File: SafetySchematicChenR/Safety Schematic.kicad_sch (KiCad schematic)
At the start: 48 parts, among them J1 XT60-M, J2 430450200, J3 Conn_01x04_Pin, J4 22035035, J5 430450200, J6 430450200, J7 XT60-M, K1 Fujitsu_FTR-LYAA005x, Q1 IRLML6344TRPBF, U1 74AHC1G32, U10 MCP2562-E/P, U11 74AHC1G08, U12 MCP6286T-E/OT, U13 MAX603, U2 74LVC1GU04DRL, U3 LT1962-3, U4 MAX603, U5 74LVC1GU04DRL, U6 Inverter_Schmitt_Dual, U7 74LS279, U8 74LVC1GU04DRL

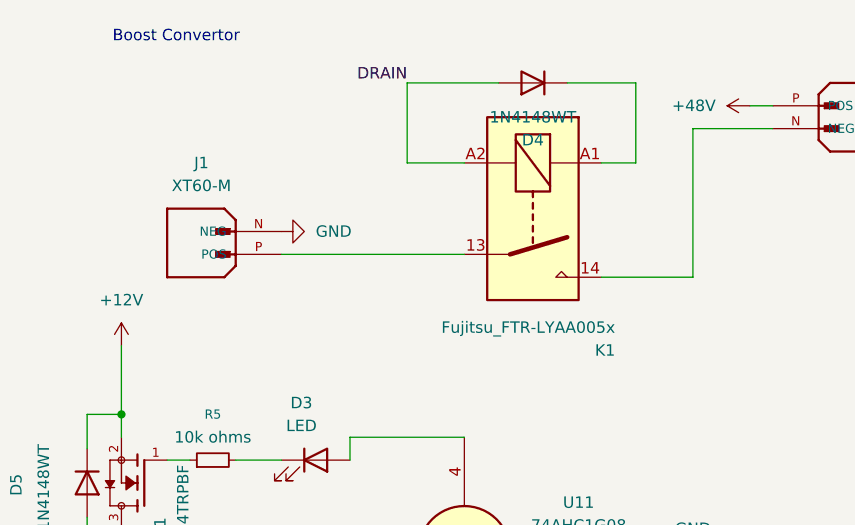
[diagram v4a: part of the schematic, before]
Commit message: replaced relay
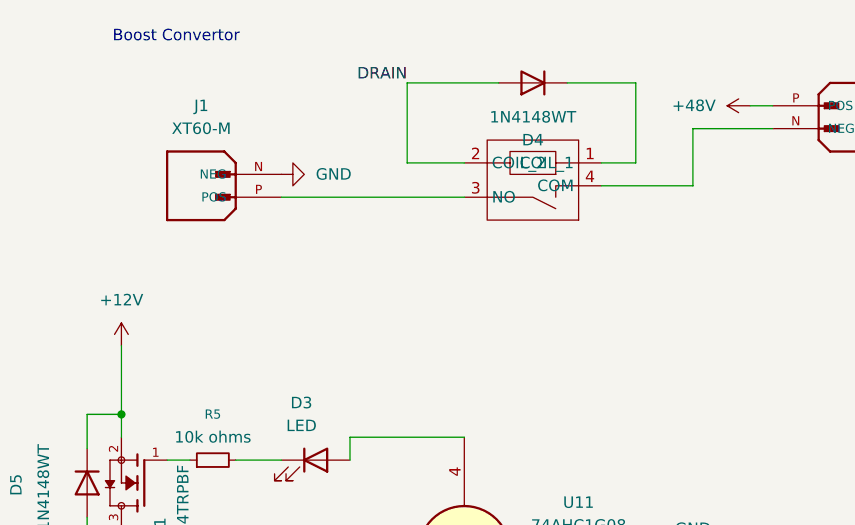
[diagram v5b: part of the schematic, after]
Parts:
- removed K1: Fujitsu_FTR-LYAA005x, Relay_THT:Relay_SPST-NO_Fujitsu_FTR-LYAA005x_FormA_Vertical, symbol Relay:Fujitsu_FTR-LYAA005x
- added U14: J115F11AH12VDCS61.5U, SMV_ICs:J115F11AH12VDCS615U, symbol SMV_Custom:J115F11AH12VDCS61.5U
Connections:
- net DRAIN: now also U14.2 (COIL_2)
- net at D4.1 (K): now also U14.1 (COIL_1)
- net at J1.P (POS): now also U14.3 (NO)
- net at J7.N (NEG): now also U14.4 (COM)
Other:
- moved on the sheet: J1
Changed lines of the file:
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@@
 	(wire
 		(pts
-			(xy 81.28 41.91) (xy 81.28 25.4)
+			(xy 81.28 31.75) (xy 81.28 25.4)
 		)
 		(stroke
@@
 	(wire
 		(pts
-			(xy 71.12 41.91) (xy 81.28 41.91)
+			(xy 71.12 31.75) (xy 81.28 31.75)
 		)
 		(stroke
@@
 	(wire
 		(pts
-			(xy 35.56 39.37) (xy 55.88 39.37)
+			(xy 35.56 33.02) (xy 55.88 33.02)
 		)
 		(stroke
@@
 	(symbol
 		(lib_id "power:GND")
-		(at 35.56 36.83 90)
+		(at 35.56 30.48 90)
 		(unit 1)
 		(exclude_from_sim no)
@@
 		(fields_autoplaced yes)
 		(property "Reference" "#PWR010"
-			(at 41.91 36.83 0)
+			(at 41.91 30.48 0)
 			(effects
 				(font
@@
 		)
 		(property "Value" "GND"
-			(at 39.37 36.8299 90)
+			(at 39.37 30.4799 90)
 			(effects
 				(font
@@
 		)
 		(property "Footprint" ""
-			(at 35.56 36.83 0)
+			(at 35.56 30.48 0)
 			(effects
 				(font
@@
 		)
 		(property "Datasheet" ""
-			(at 35.56 36.83 0)
+			(at 35.56 30.48 0)
 			(effects
 				(font
@@
 		)
 		(property "Description" "Power symbol creates a global label with name \"GND\" , ground"
-			(at 35.56 36.83 0)
+			(at 35.56 30.48 0)
 			(effects
 				(font
@@
 	(symbol
 		(lib_id "SMV_Custom:XT60-M")
-		(at 30.48 36.83 180)
+		(at 30.48 30.48 180)
 		(unit 1)
 		(exclude_from_sim no)
@@
 		(fields_autoplaced yes)
 		(property "Reference" "J1"
-			(at 26.67 29.21 0)
+			(at 26.67 22.86 0)
 			(effects
 				(font
@@
 		)
 		(property "Value" "XT60-M"
-			(at 26.67 31.75 0)
+			(at 26.67 25.4 0)
 			(effects
 				(font
@@
 		)
 		(property "Footprint" "SMV_Connectors:AMASS_XT60-M"
-			(at 30.48 36.83 0)
+			(at 30.48 30.48 0)
 			(effects
 				(font
@@
 		)
 		(property "Datasheet" ""
-			(at 30.48 36.83 0)
+			(at 30.48 30.48 0)
 			(effects
 				(font
@@
 		)
 		(property "Description" ""
-			(at 30.48 36.83 0)
+			(at 30.48 30.48 0)
 			(effects
 				(font
@@
 		)
 		(property "MF" "AMASS"
-			(at 30.48 36.83 0)
+			(at 30.48 30.48 0)
 			(effects
 				(font
@@
 		)
 		(property "MAXIMUM_PACKAGE_HEIGHT" "16.00 mm"
-			(at 30.48 36.83 0)
+			(at 30.48 30.48 0)
 			(effects
 				(font
@@
 		)
 		(property "Package" "Package"
-			(at 30.48 36.83 0)
+			(at 30.48 30.48 0)
 			(effects
 				(font
@@
 		)
 		(property "Price" "None"
-			(at 30.48 36.83 0)
+			(at 30.48 30.48 0)
 			(effects
 				(font
@@
 		)
 		(property "Check_prices" "https://www.snapeda.com/parts/XT60-M/AMASS/view-part/?ref=eda"
-			(at 30.48 36.83 0)
+			(at 30.48 30.48 0)
 			(effects
 				(font
@@
 		)
 		(property "STANDARD" "IPC 7351B"
-			(at 30.48 36.83 0)
+			(at 30.48 30.48 0)
 			(effects
 				(font
@@
 		)
 		(property "PARTREV" "V1.2"
-			(at 30.48 36.83 0)
+			(at 30.48 30.48 0)
 			(effects
 				(font
@@
 		)
 		(property "SnapEDA_Link" "https://www.snapeda.com/parts/XT60-M/AMASS/view-part/?ref=snap"
-			(at 30.48 36.83 0)
+			(at 30.48 30.48 0)
 			(effects
 				(font
@@
 		)
 		(property "MP" "XT60-M"
-			(at 30.48 36.83 0)
+			(at 30.48 30.48 0)
 			(effects
 				(font
@@
 		)
 		(property "Description_1" "\n                        \n                            Plug; DC supply; XT60; male; PIN: 2; for cable; soldered; 30A; 500V\n                        \n"
-			(at 30.48 36.83 0)
+			(at 30.48 30.48 0)
 			(effects
 				(font
@@
 		)
 		(property "Availability" "Not in stock"
-			(at 30.48 36.83 0)
+			(at 30.48 30.48 0)
 			(effects
 				(font
@@
 		)
 		(property "MANUFACTURER" "AMASS"
-			(at 30.48 36.83 0)
+			(at 30.48 30.48 0)
 			(effects
 				(font
@@
 	)
 	(symbol
-		(lib_id "Relay:Fujitsu_FTR-LYAA005x")
-		(at 63.5 34.29 270)
-		(unit 1)
-		(exclude_from_sim no)
-		(in_bom yes)
-		(on_board yes)
-		(dnp no)
-		(property "Reference" "K1"
-			(at 72.644 50.038 90)
-			(effects
-				(font
-					(size 1.27 1.27)
-				)
-				(justify right)
-			)
-		)
-		(property "Value" "Fujitsu_FTR-LYAA005x"
-			(at 72.644 47.498 90)
-			(effects
-				(font
-					(size 1.27 1.27)
-				)
-				(justify right)
-			)
-		)
-		(property "Footprint" "Relay_THT:Relay_SPST-NO_Fujitsu_FTR-LYAA005x_FormA_Vertical"
-			(at 62.23 45.72 0)
-			(effects
-				(font
-					(size 1.27 1.27)
-				)
-				(justify left)
-				(hide yes)
-			)
-		)
-		(property "Datasheet" "https://www.fujitsu.com/sg/imagesgig5/ftr-ly.pdf"
-			(at 59.69 52.07 0)
-			(effects
-				(font
-					(size 1.27 1.27)
-				)
-				(justify left)
-				(hide yes)
-			)
-		)
-		(property "Description" "Relay, SPST Form A, vertical mount, 5-60V coil, 6A, 250VAC, 28 x 5 x 15mm"
-			(at 63.5 34.29 0)
-			(effects
-				(font
-					(size 1.27 1.27)
-				)
-				(hide yes)
-			)
-		)
-		(pin "A2"
-		)
-		(pin "13"
-		)
-		(pin "A1"
-		)
-		(pin "14"
-		)
-		(instances
-			(project ""
-				(path "/927e5849-97d5-445f-9a77-6290d281bda7"
-					(reference "K1")
-					(unit 1)
-				)
-			)
-		)
-	)
-	(symbol
 		(lib_id "74xGxx:74AHC1G08")
 		(at 55.88 72.39 90)
@@
 					(unit 1)
 				)
+			)
+		)
+	)
+	(symbol
+		(lib_id "SMV_Custom:J115F11AH12VDCS61.5U")
+		(at 63.5 31.75 180)
+		(unit 1)
+		(exclude_from_sim no)
+		(in_bom yes)
+		(on_board yes)
+		(dnp no)
+		(fields_autoplaced yes)
+		(property "Reference" "U14"
+			(at 50.292 31.242 90)
+			(effects
+				(font
+					(size 1.27 1.27)
+				)
+				(hide yes)
+			)
+		)
+		(property "Value" "J115F11AH12VDCS61.5U"
+			(at 52.832 31.242 90)
+			(effects
+				(font
+					(size 1.27 1.27)
+				)
+				(hide yes)
+			)
+		)
+		(property "Footprint" "SMV_ICs:J115F11AH12VDCS615U"
+			(at 63.5 31.75 0)
+			(effects
+				(font
+					(size 1.27 1.27)
+				)
+				(hide yes)
+			)
+		)
+		(property "Datasheet" ""
+			(at 63.5 31.75 0)
+			(effects
+				(font
+					(size 1.27 1.27)
+				)
+				(hide yes)
+			)
+		)
+		(property "Description" ""
+			(at 63.5 31.75 0)
+			(effects
+				(font
+					(size 1.27 1.27)
+				)
+				(hide yes)
+			)
+		)
+		(pin "1"
+		)
+		(pin "4"
+		)
+		(pin "2"
+		)
+		(pin "3"
+		)
+		(instances
+			(project ""
+				(path "/927e5849-97d5-445f-9a77-6290d281bda7"
+					(reference "U14")
+					(unit 1)
+				)

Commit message: Changed sm things
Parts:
- removed R5: 10k ohms, symbol Device:R_Small
- removed U10: MCP2562-E/P, PDIP8_300MC_MCH, symbol SMV_Custom:MCP2562-E_P
- added C12: 2 uF, symbol Device:C_Small
- added C13: 0.33 uF, symbol Device:C_Small
- added U10: LM2594HVN-12, Package_DIP:DIP-8_W7.62mm, symbol Regulator_Switching:LM2594HVN-12
- added U15: MCP2562-E-P, Package_DIP:DIP-8_W7.62mm, symbol Interface_CAN_LIN:MCP2562-E-P
- C1, C10, C11, C2, C3, C4, C6, C8: value 10 uF -> 0.1 uF
- C5, C9: value 10 uF -> 0.33 uF
- C7: value 10 uF -> 0.01 uF
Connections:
- net +12V: now also C13.1, U10.4 (FB), U10.8 (OUT)
- net +3V0: now also C7.1, U3.2 (SENSE)
- net +48V: now also U14.4 (COM); no longer J7.P (POS)
- net +5V: now also U15.3 (VDD), U15.5 (Vio)
- net CANIN: now also U15.1 (TXD)
- net CANOUT: now also U15.4 (RXD)
- net GND: now also J7.N (NEG), C12.2, C13.2, U10.5 (~{ON}/OFF), U10.6 (GND), U15.2 (VSS), U15.8 (STBY); no longer C7.2, U3.2 (SENSE)
- net at Q1.1: now also D3.1 (K)
- net at J4.3, R10.1: now also U15.6 (CANL)
- net at J4.1, R10.2: now also U15.7 (CANH)
- net at U3.3 (BYP): now also C7.2; no longer C7.1
- new net: C12.1, J7.P (POS), U10.7 (VIN)
- no-connect marks 57 -> 60
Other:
- moved on the sheet: C1, C2, C3, C7, J7

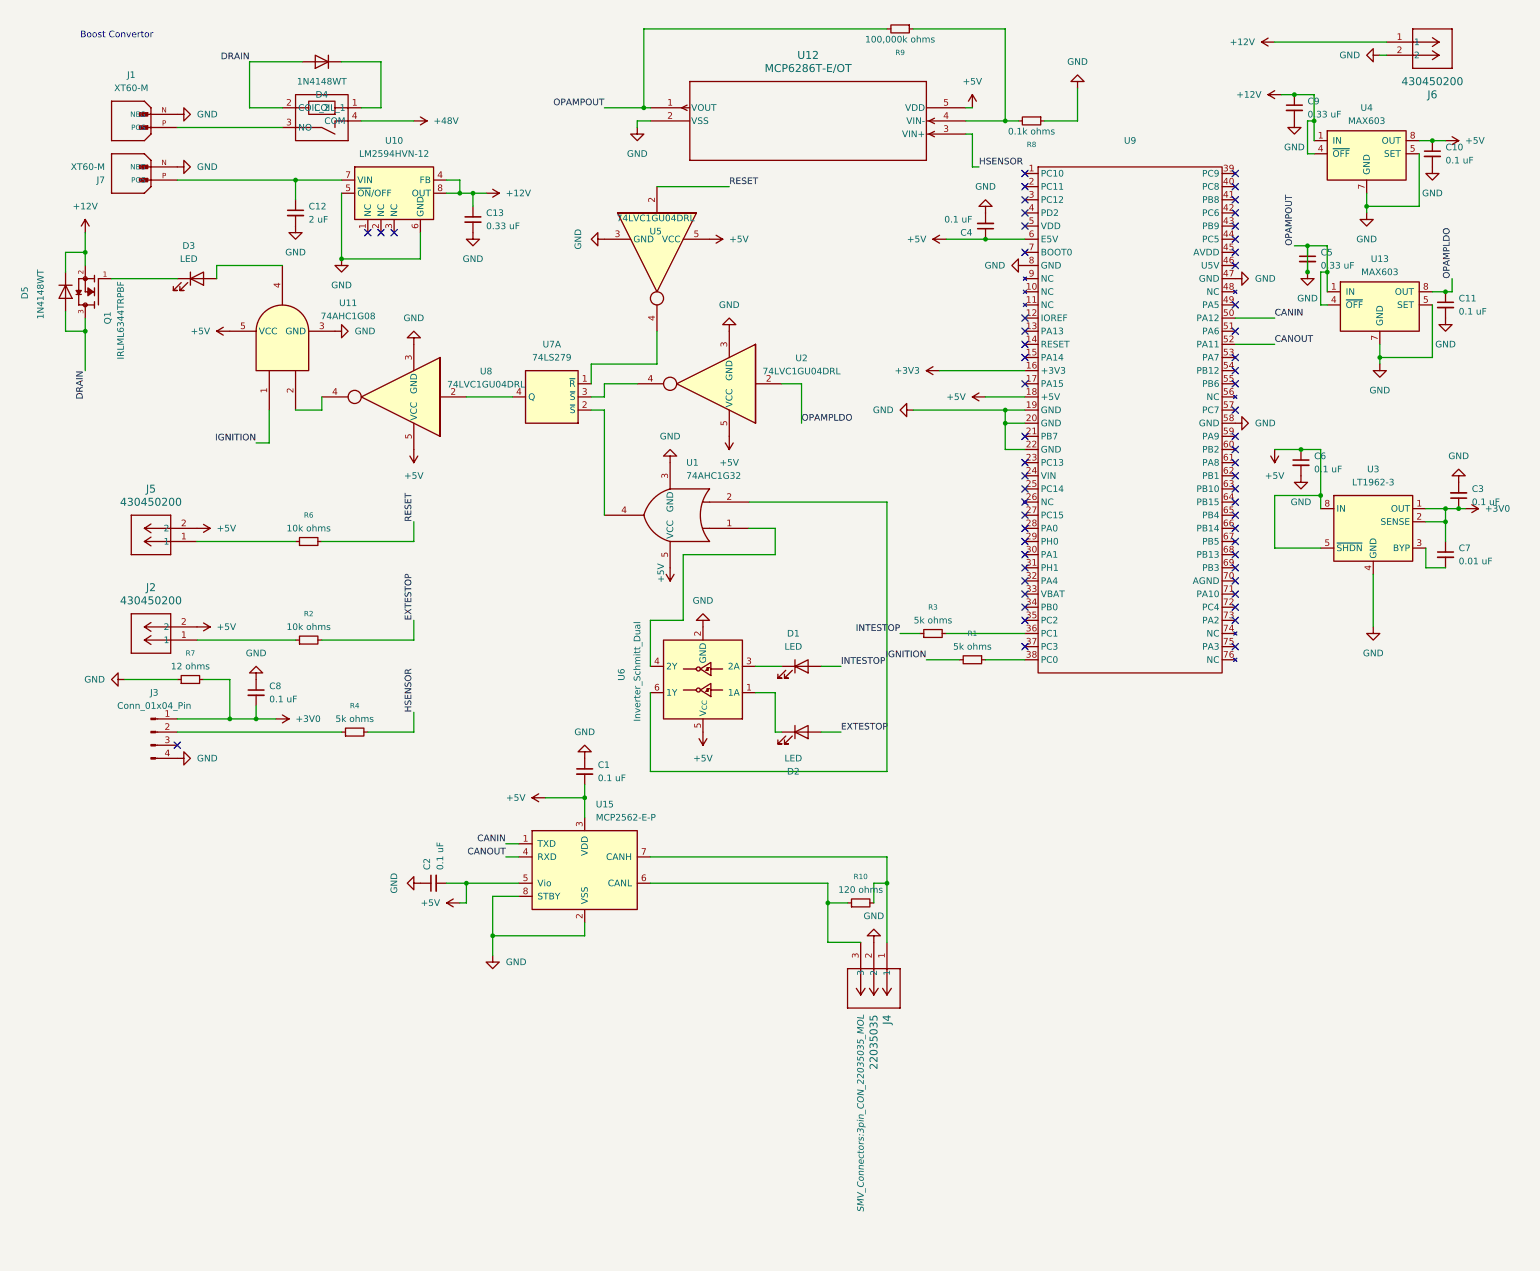
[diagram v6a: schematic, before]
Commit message: added test points and removed unused 3V3 tag
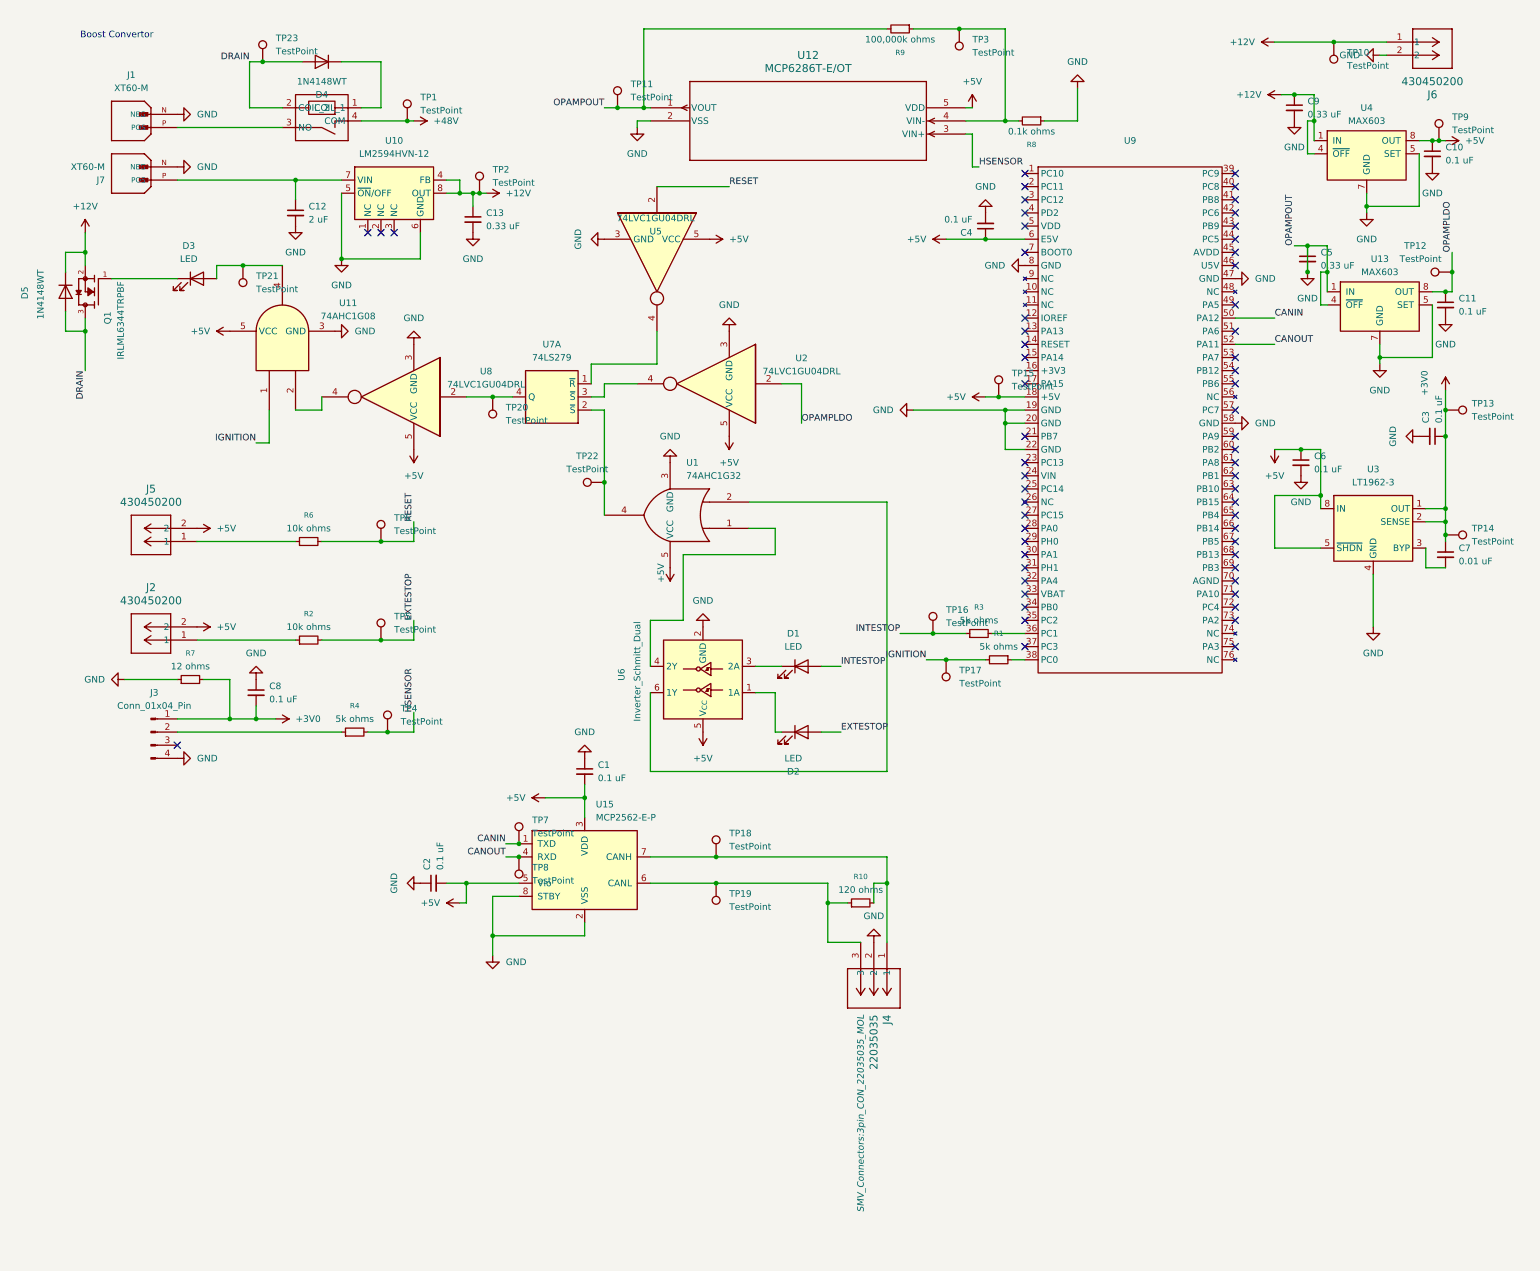
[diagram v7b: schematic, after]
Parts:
- added TP1, TP10, TP11, TP12, TP13, TP14, TP15, TP16, TP17, TP18, TP19, TP2, TP20, TP21, TP22, TP23, TP3, TP4, TP5, TP6, TP7, TP8, TP9: TestPoint, symbol Connector:TestPoint
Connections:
- net +12V: now also TP10.1, TP2.1
- net +3V0: now also TP13.1, TP14.1
- net +48V: now also TP1.1
- net +5V: now also TP15.1, TP9.1
- net CANIN: now also TP7.1
- net CANOUT: now also TP8.1
- net DRAIN: now also TP23.1
- net EXTESTOP: now also TP5.1
- net GND: now also TP11.1
- net HSENSOR: now also TP4.1
- net IGNITION: now also TP17.1
- net INTESTOP: now also TP16.1
- net OPAMPLDO: now also TP12.1
- net RESET: now also TP6.1
- net at R8.2, R9.1, U12.4 (VIN-): now also TP3.1
- net at J4.3, R10.1, U15.6 (CANL): now also TP19.1
- net at J4.1, R10.2, U15.7 (CANH): now also TP18.1
- net at D3.2 (A), U11.4: now also TP21.1
- net at U7.4 (Q), U8.2: now also TP20.1
- net at U1.4, U7.2 (~{S}): now also TP22.1
- net +3V3: no longer names the net of U9.16 (+3V3)
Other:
- moved on the sheet: C3, R1, R3

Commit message: finished changes for 2nd feedback round
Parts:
- removed C13: 0.33 uF, symbol Device:C_Small
- removed D5: 1N4148WT, Diode_SMD:D_SOD-523, symbol Diode:1N4148WT
- removed J5: 430450200, SMV_Connectors:CONN_SD-43045-001_02_MOL, symbol SMV_Custom:430450200
- removed R1, R3, R4: 5k ohms, symbol Device:R_Small
- removed R7: 12 ohms, symbol Device:R_Small
- removed TP12: TestPoint, symbol Connector:TestPoint
- removed U10: LM2594HVN-12, Package_DIP:DIP-8_W7.62mm, symbol Regulator_Switching:LM2594HVN-12
- removed U11: 74AHC1G08, symbol 74xGxx:74AHC1G08
- removed U13: MAX603, symbol Regulator_Linear:MAX603
- removed U5: 74LVC1GU04DRL, Package_TO_SOT_SMD:SOT-553, symbol 74xGxx:74LVC1GU04DRL
- removed U6: Inverter_Schmitt_Dual, symbol 74xGxx:Inverter_Schmitt_Dual
- added D5: 7.5V, Diode_SMD:D_MiniMELF, symbol Diode:BZV55C7V5
- added R11: 20k ohms, symbol Device:R_Small
- added R12, R13: 5k ohms, symbol Device:R_Small
- added R14: 10k ohms, symbol Device:R_Small
- added R5: 10 ohms, symbol Device:R_Small
- added U10: 74LVC1GU04DRL, Package_TO_SOT_SMD:SOT-553, symbol 74xGxx:74LVC1GU04DRL
- added U5: LT1962-3.3, Package_SO:MSOP-8_3x3mm_P0.65mm, symbol Regulator_Linear:LT1962-3.3
- C12: value 2 uF -> 0.01 uF
- C5: value 0.33 uF -> 0.1 uF
- R6: value 10k ohms -> 5k ohms
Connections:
- net +12V: now also R11.1; no longer Q1.2, TP2.1
- net +48V: now also J7.P (POS)
- net +5V: now also U10.5 (VCC); no longer C2.2, U15.5 (Vio)
- net DRAIN: now also Q1.2, R5.1; no longer Q1.3, U14.2 (COIL_2)
- net GND: now also R6.2, U14.2 (COIL_2), R12.2, R13.2, R14.2, U10.3 (GND), U5.4 (GND); no longer C12.2, C5.1, R9.2, TP11.1, U12.1 (VOUT)
- net HSENSOR: now also J3.2 (Pin_2)
- net IGNITION: now also U9.38 (PC0)
- net INTESTOP: now also U9.36 (PC1)
- net RESET: now also U7.1 (~{R}), U9.35 (PC2), R13.1; no longer R6.2, TP6.1
- net RELAYSENSOR: now reaches U9.28 (PA0)
- net RELAYSENSOR: now also C11.1, C12.1, TP2.1, TP6.1, U5.1 (OUT), U5.2 (SENSE)
- net RELAY: now reaches D4.1 (K), U14.1 (COIL_1)
- net RELAY: now also C5.1, U5.5 (~{SHDN}), U5.8 (IN)
- net at D3.1 (K), Q1.1: now also R5.2
- net at D3.2 (A), TP21.1: now also U8.4
- net at R6.1: now also D2.1 (K), U10.2
- net at D1.1 (K): now also U1.1, R12.1
- net at U1.2: now also U10.4
- net OPAMPLDO renamed OPAMPOUT
- net OPAMPOUT: now also D5.2 (A); no longer C11.1
- new net: C12.2, U5.3 (BYP)
- new net: D5.1 (K), R14.1, R9.2, TP11.1, U12.1 (VOUT)
- new net: Q1.3, R11.2
- new net +3V3: C2.2, U15.5 (Vio)
- no-connect marks 60 -> 55
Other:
- moved on the sheet: C1, C2, C3, C6, C7, C8, D1, D2, D3, J2, J3, J4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
